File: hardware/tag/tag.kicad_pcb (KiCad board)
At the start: 2 copper layers, 94 x 45.7 mm, 8 parts

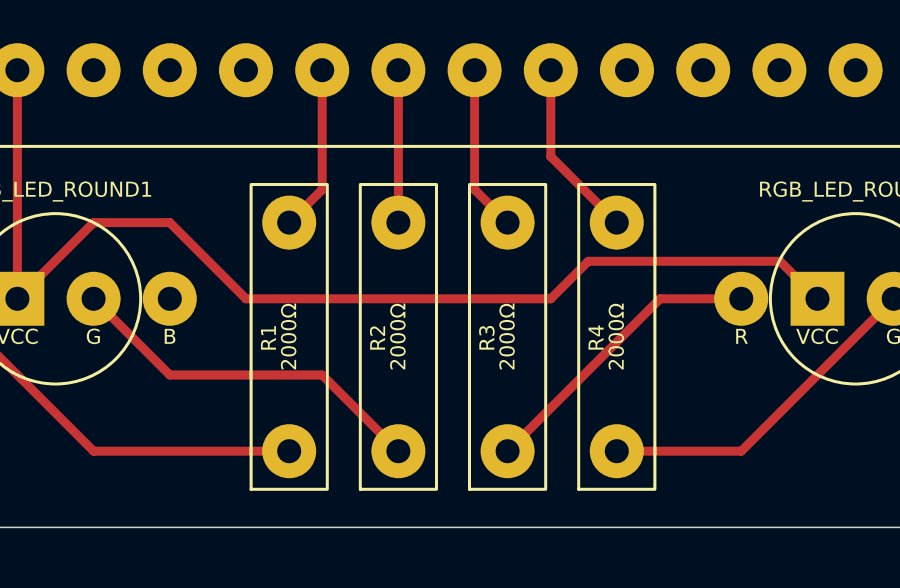
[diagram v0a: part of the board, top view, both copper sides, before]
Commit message: hardware: Add more footprint measurement.
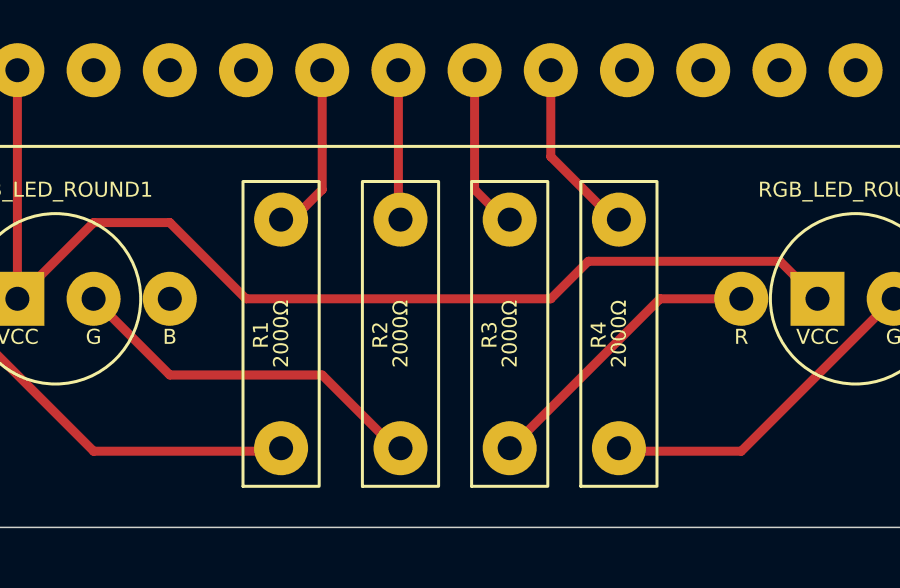
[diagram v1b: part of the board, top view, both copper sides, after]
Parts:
- moved R1 0.29 mm to (132.1, 115.6)
- moved R2 0.12 mm to (136.1, 115.6)
- moved R3 0.12 mm to (139.7, 115.6)
- moved R4 0.12 mm to (143.3, 115.6)

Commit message: hardware: Add remote PCB.
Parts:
- added Battery_Charger1: ~, Autocam:USB-C 3.7V Lithium Battery Charger, B.Cu at (192.2, 78.7)
- added ON_OFF_SWITCH1: OFF ON, Autocam:3-PIN Switch, F.Cu at (108.0, 116.8)
- added R5: 2000Ω, Autocam:Simple Resistor, F.Cu at (143.5, 120.7)
- added RGB_LED_ROUND3: TAG_ACTIVE, Autocam:Anode RGB LED (Round), F.Cu at (163.8, 116.8)
- RGB_LED_ROUND1: value SENSOR -> BATTERY
- RGB_LED_ROUND2: value BATTERY -> SENSOR
- moved ESP32_UWB1 6.71 mm to (120.7, 78.7)
- moved RGB_LED_ROUND1 6.71 mm to (127.0, 116.8)
- moved RGB_LED_ROUND2 6.40 mm to (149.9, 116.8)
- moved 5V_DC_DC_Converter1 6.36 mm to (100.4, 111.8)
- moved R4 5.62 mm to (140.9, 120.7)
- moved R3 5.25 mm to (138.4, 120.7)
- moved R1 5.24 mm to (133.3, 120.7)
- moved R2 5.08 mm to (135.9, 120.7)
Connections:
- 5V_DC_DC_Converter1 pad 1: unconnected-(5V_DC_DC_Converter1-+-Pad1) -> Net-(Battery_Charger1-OUT+)
- 5V_DC_DC_Converter1 pad 3: unconnected-(5V_DC_DC_Converter1---Pad3) -> Net-(5V_DC_DC_Converter1---Pad3)
- ESP32_UWB1 pad 9: unconnected-(ESP32_UWB1-IO15-Pad9) -> Net-(ESP32_UWB1-IO15)
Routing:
- net Net-(Battery_Charger1-OUT-): track 0.00 -> 87.5 mm
- net Net-(Battery_Charger1-OUT+): track 0.00 -> 71.1 mm
- net Net-(RGB_LED_ROUND3-B): track 0.00 -> 25.7 mm
- net Net-(ESP32_UWB1-3V3): track 37.4 -> 46.5 mm
- net Net-(5V_DC_DC_Converter1---Pad3): track 0.00 -> 8.71 mm
- net Net-(ESP32_UWB1-IO15): track 0.00 -> 4.90 mm
- net Net-(RGB_LED_ROUND1-G): track 12.3 -> 9.17 mm
- net Net-(RGB_LED_ROUND1-R): track 13.7 -> 11.7 mm
- net Net-(5V_DC_DC_Converter1---Pad5): track 18.5 -> 19.8 mm
- net Net-(ESP32_UWB1-5V0): track 18.5 -> 19.8 mm
- net Net-(ESP32_UWB1-IO14): track 6.50 -> 5.48 mm
- net Net-(ESP32_UWB1-IO2): track 5.54 -> 4.86 mm
- net Net-(RGB_LED_ROUND2-R): track 9.89 -> 9.27 mm
- net Net-(ESP32_UWB1-IO13): track 5.54 -> 4.93 mm
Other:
- board size 94 x 45.7 mm -> 96.5 x 48.3 mm

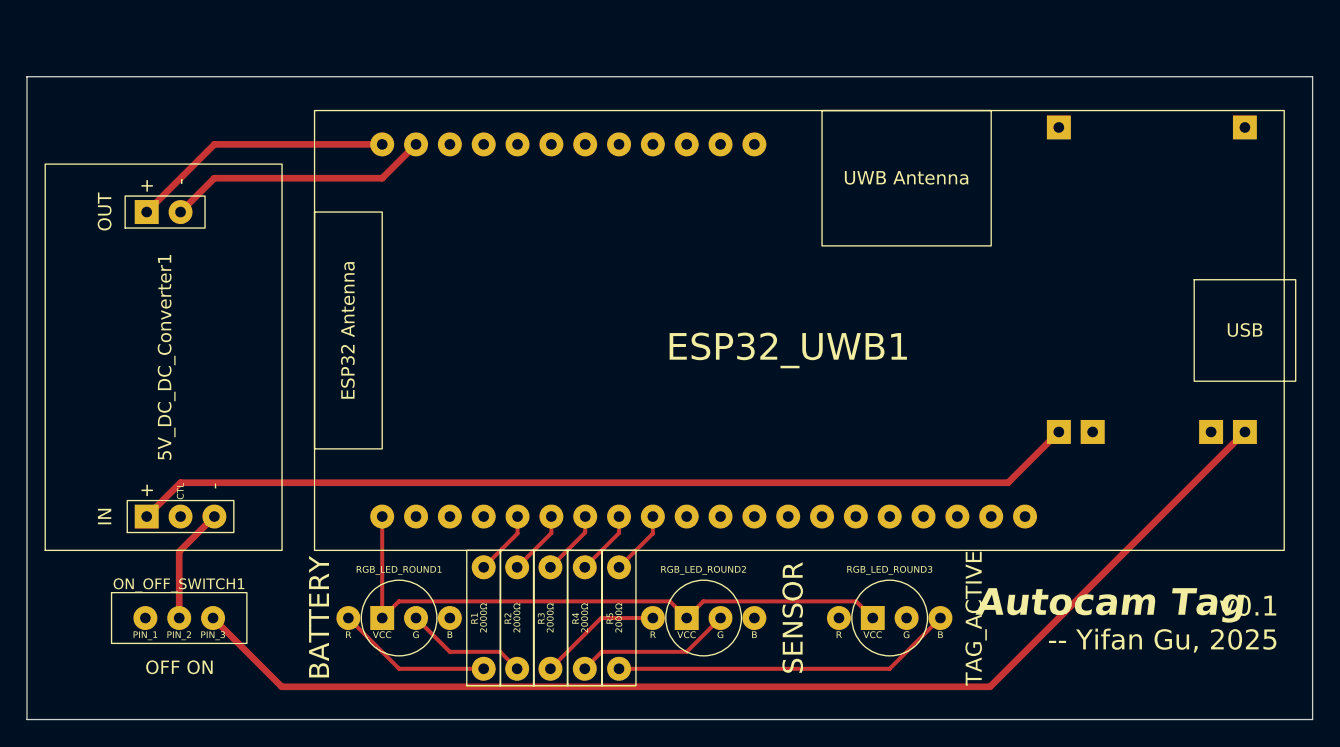
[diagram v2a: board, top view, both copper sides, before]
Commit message: remote: Add battery status LED logic.
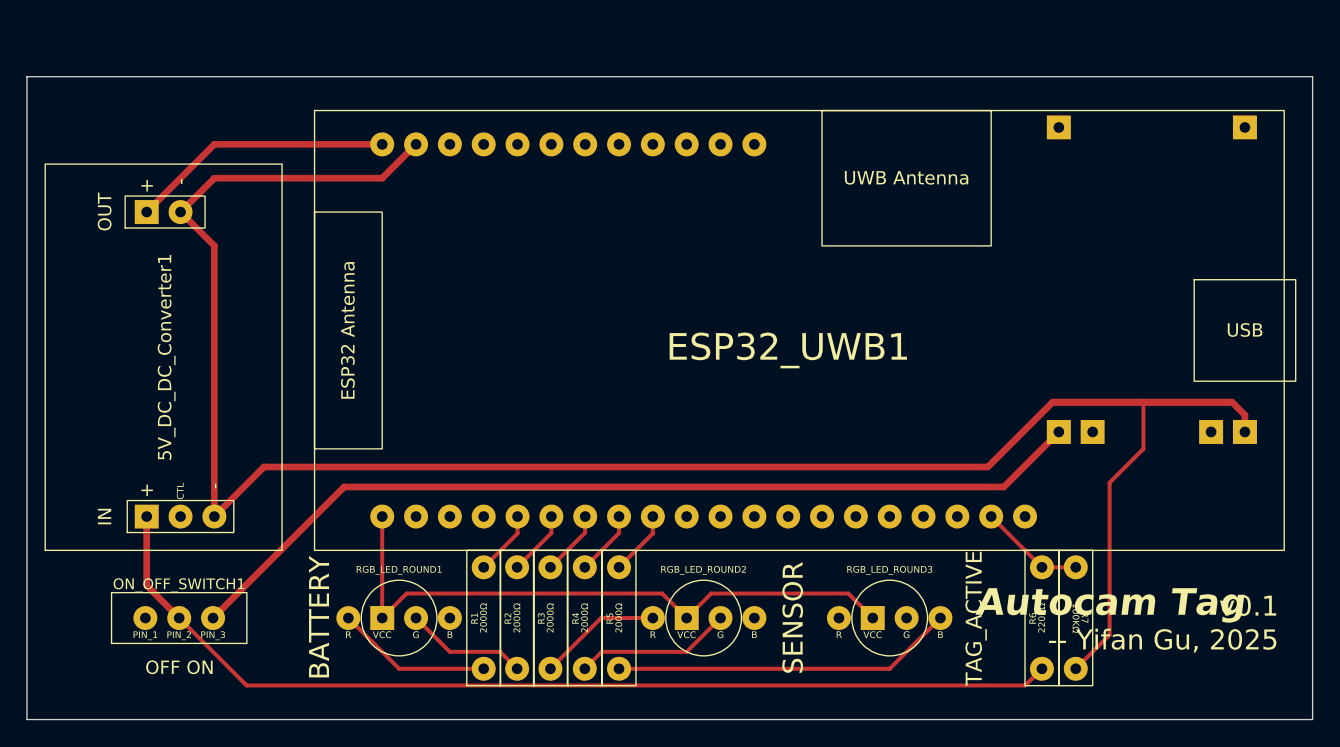
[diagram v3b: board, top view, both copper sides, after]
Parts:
- added R6: 220KΩ, Autocam:Simple Resistor, F.Cu at (175.3, 120.7)
- added R7: 100KΩ, Autocam:Simple Resistor, F.Cu at (177.8, 113.0)
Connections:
- 5V_DC_DC_Converter1 pad 1: Net-(Battery_Charger1-OUT+) -> Net-(5V_DC_DC_Converter1-+-Pad1)
- 5V_DC_DC_Converter1 pad 3: Net-(5V_DC_DC_Converter1---Pad3) -> Net-(Battery_Charger1-OUT-)
- 5V_DC_DC_Converter1 pad 5: Net-(5V_DC_DC_Converter1---Pad5) -> Net-(Battery_Charger1-OUT-)
- ESP32_UWB1 pad 19: unconnected-(ESP32_UWB1-IO36-Pad19) -> Net-(ESP32_UWB1-IO36)
- ESP32_UWB1 pad 22: Net-(5V_DC_DC_Converter1---Pad5) -> Net-(Battery_Charger1-OUT-)
- ON_OFF_SWITCH1 pad 2: Net-(5V_DC_DC_Converter1---Pad3) -> Net-(5V_DC_DC_Converter1-+-Pad1)
- ON_OFF_SWITCH1 pad 3: Net-(Battery_Charger1-OUT-) -> Net-(Battery_Charger1-OUT+)
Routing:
- net Net-(5V_DC_DC_Converter1-+-Pad1): track 0.00 -> 76.0 mm
- net Net-(Battery_Charger1-OUT-): track 87.5 -> 161.9 mm
- net Net-(5V_DC_DC_Converter1---Pad5): track 19.8 -> 0.00 mm
- net Net-(5V_DC_DC_Converter1---Pad3): track 8.71 -> 0.00 mm
- net Net-(ESP32_UWB1-IO36): track 0.00 -> 7.93 mm
- net Net-(Battery_Charger1-OUT+): track 71.1 -> 69.3 mm
- net Net-(ESP32_UWB1-3V3): track 46.5 -> 47.5 mm
